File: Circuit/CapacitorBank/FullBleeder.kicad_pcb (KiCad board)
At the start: 2 copper layers, 76.2 x 86.4 mm, 19 parts, among them J1 Signal 1/3, J2 Signal 2/4, J3 Power

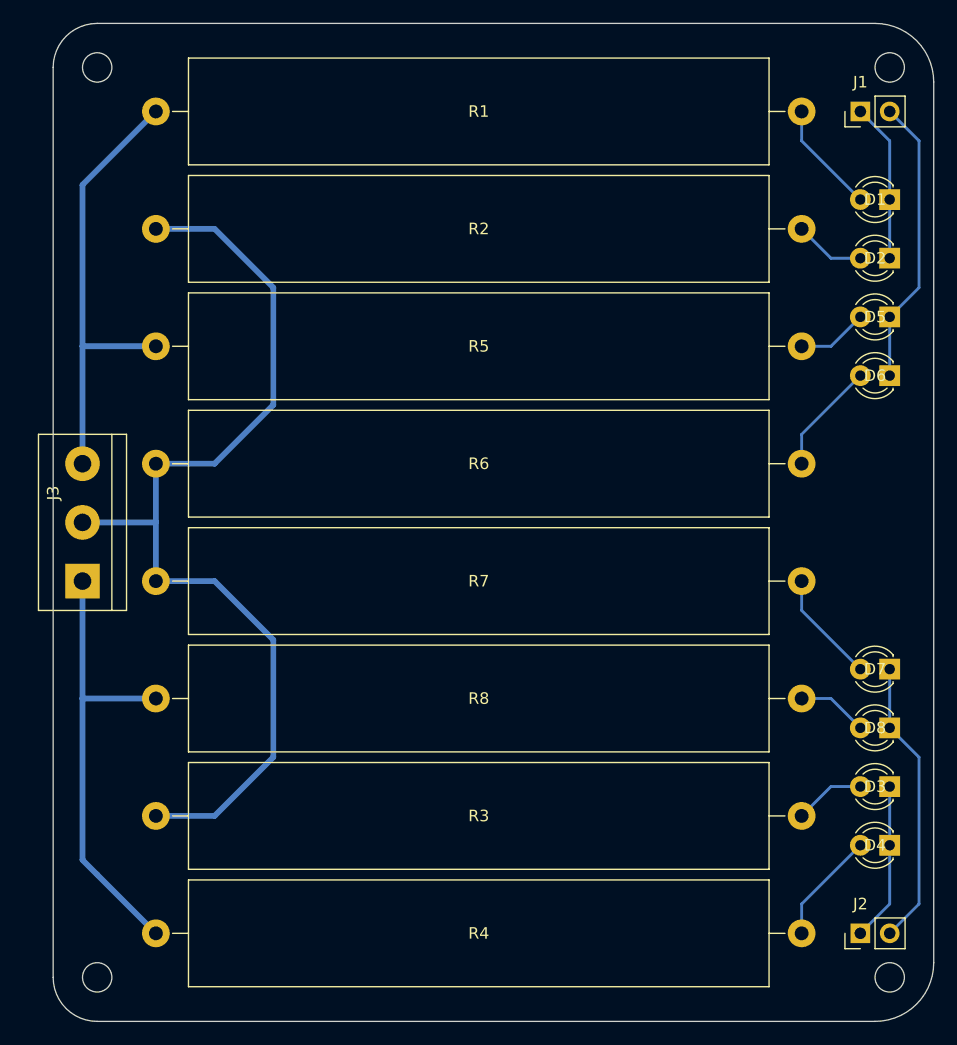
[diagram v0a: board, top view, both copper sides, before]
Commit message: [Circuit] Polarized capacitor bank and bleeder
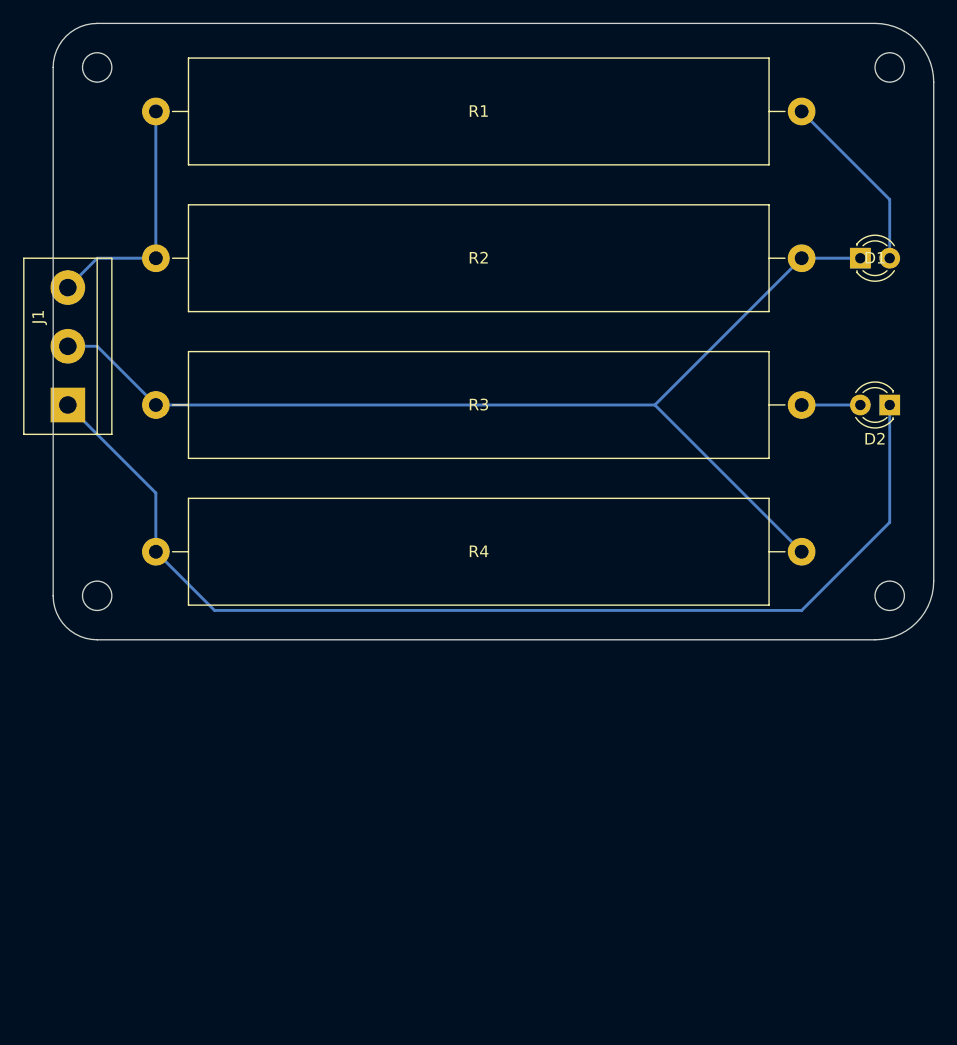
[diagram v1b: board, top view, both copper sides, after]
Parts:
- removed D3, D4, D5, D6, D7, D8: LED, LED_THT:LED_D3.0mm_FlatTop
- removed the J1 at (121.9, 61.0)
- removed J2: Signal 2/4, Connector_PinHeader_2.54mm:PinHeader_1x02_P2.54mm_Vertical
- removed the R2 at (116.8, 71.1)
- removed the R4 at (116.8, 132.1)
- removed R6, R8: 20K, Resistor_THT:R_Axial_Power_L50.0mm_W9.0mm_P55.88mm
- R1, R3: value 20K -> 40K/5W
- R2: renamed from R5; value 20K -> 20K/10W
- R4: renamed from R7; value 20K -> 20K/10W
- moved R4 55.9 mm to (116.8, 99.1), turned to 180 degrees
- moved R3 35.6 mm to (61.0, 86.4)
- moved J1 15.3 mm to (53.3, 86.4)
- moved D2 12.7 mm to (124.5, 86.4)
- moved R2 7.62 mm to (61.0, 73.7)
- moved D1 5.68 mm to (121.9, 73.7), turned to 0 degrees
- renumbered J3 to J1
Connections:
- net +VDC renamed /CapacitorPower+
- D1 pad 1: Net-(D1-Pad1) -> /CapacitorCenter
- D2 pad 1: Net-(D1-Pad1) -> /CapacitorPower-
- J1 pad 1: -VDC -> /CapacitorPower-
- J1 pad 2: GND -> /CapacitorCenter
- R2 pad 2: Net-(D5-Pad2) -> /CapacitorCenter
- R3 pad 1: GND -> /CapacitorCenter
- R3 pad 2: Net-(D3-Pad2) -> Net-(D2-Pad2)
- R4 pad 1: GND -> /CapacitorCenter
- R4 pad 2: Net-(D7-Pad2) -> /CapacitorPower-
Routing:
- net /CapacitorPower-: track 0.00 -> 94.8 mm
- net /CapacitorCenter: track 0.00 -> 93.9 mm
- net GND: track 85.9 -> 0.00 mm
- net -VDC: track 39.5 -> 0.00 mm
- net Net-(D7-Pad1): track 25.0 -> 0.00 mm
- net Net-(D5-Pad1): track 25.0 -> 0.00 mm
- net /CapacitorPower+: track 39.5 -> 21.4 mm
- net Net-(D3-Pad1): track 13.8 -> 0.00 mm
- net Net-(D1-Pad1): track 13.8 -> 0.00 mm
- net Net-(D4-Pad2): track 9.72 -> 0.00 mm
- net Net-(D7-Pad2): track 9.72 -> 0.00 mm
- net Net-(D6-Pad2): track 9.72 -> 0.00 mm
- net Net-(D3-Pad2): track 6.13 -> 0.00 mm
- net Net-(D5-Pad2): track 6.13 -> 0.00 mm
- net Net-(D1-Pad2): track 9.72 -> 15.9 mm
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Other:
- board size 76.2 x 86.4 mm -> 76.2 x 53.3 mm

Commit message: [Circuit] Update the numbers in capacitor bank subsystem
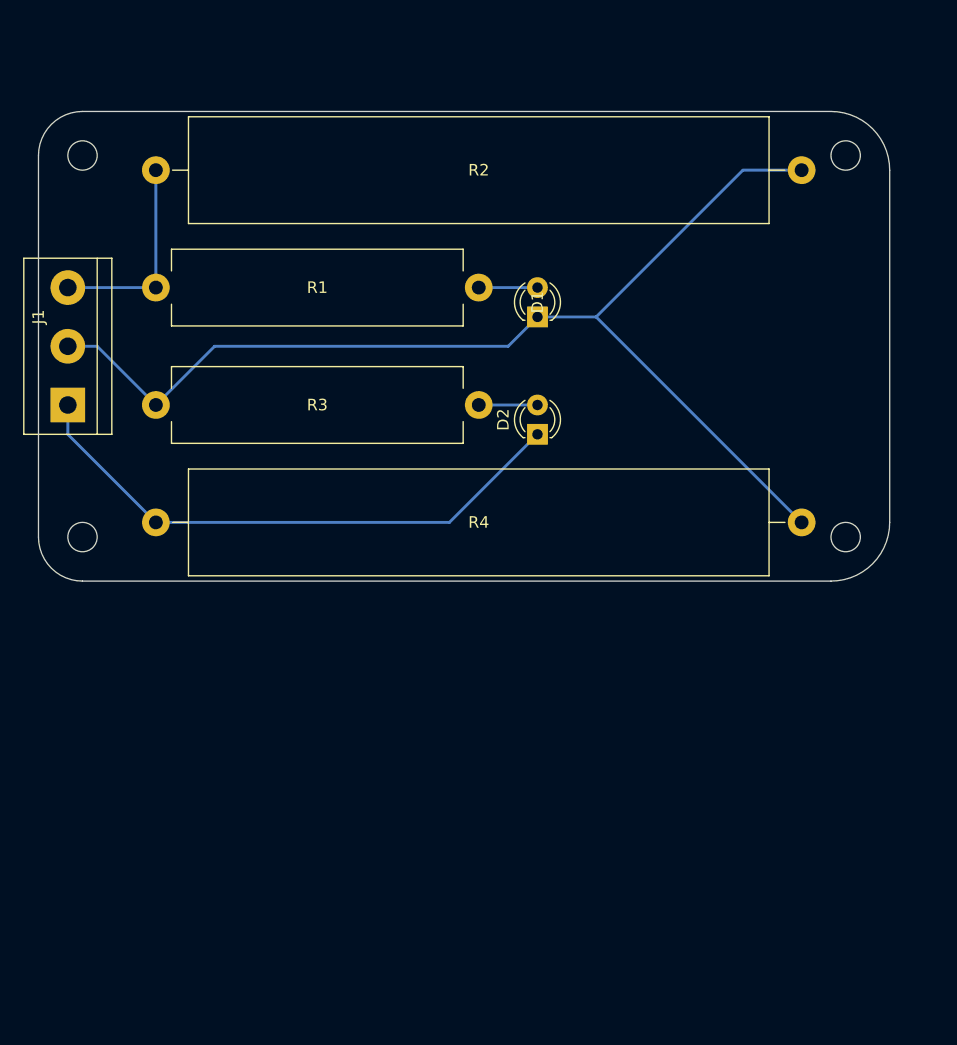
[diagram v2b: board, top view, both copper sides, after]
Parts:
- R1, R3: value 40K/5W -> 43K/5W; footprint Resistor_THT:R_Axial_Power_L50.0mm_W9.0mm_P55.88mm -> Resistor_THT:R_Axial_Power_L25.0mm_W6.4mm_P27.94mm
- moved D2 30.6 mm to (94.0, 88.9), turned to 90 degrees
- moved D1 28.4 mm to (94.0, 78.7), turned to 90 degrees
- moved R1 15.2 mm to (61.0, 76.2)
- moved R2 7.62 mm to (61.0, 66.0)
- moved R4 2.54 mm to (116.8, 96.5)
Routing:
- net /CapacitorPower-: track 94.8 -> 49.5 mm
- net Net-(D1-Pad2): track 15.9 -> 5.08 mm
- net /CapacitorCenter: track 93.9 -> 99.2 mm
- net /CapacitorPower+: track 21.4 -> 17.8 mm
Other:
- board size 76.2 x 53.3 mm -> 73.7 x 40.6 mm

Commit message: [Circuit] Add isolated switches to bleeder circuits
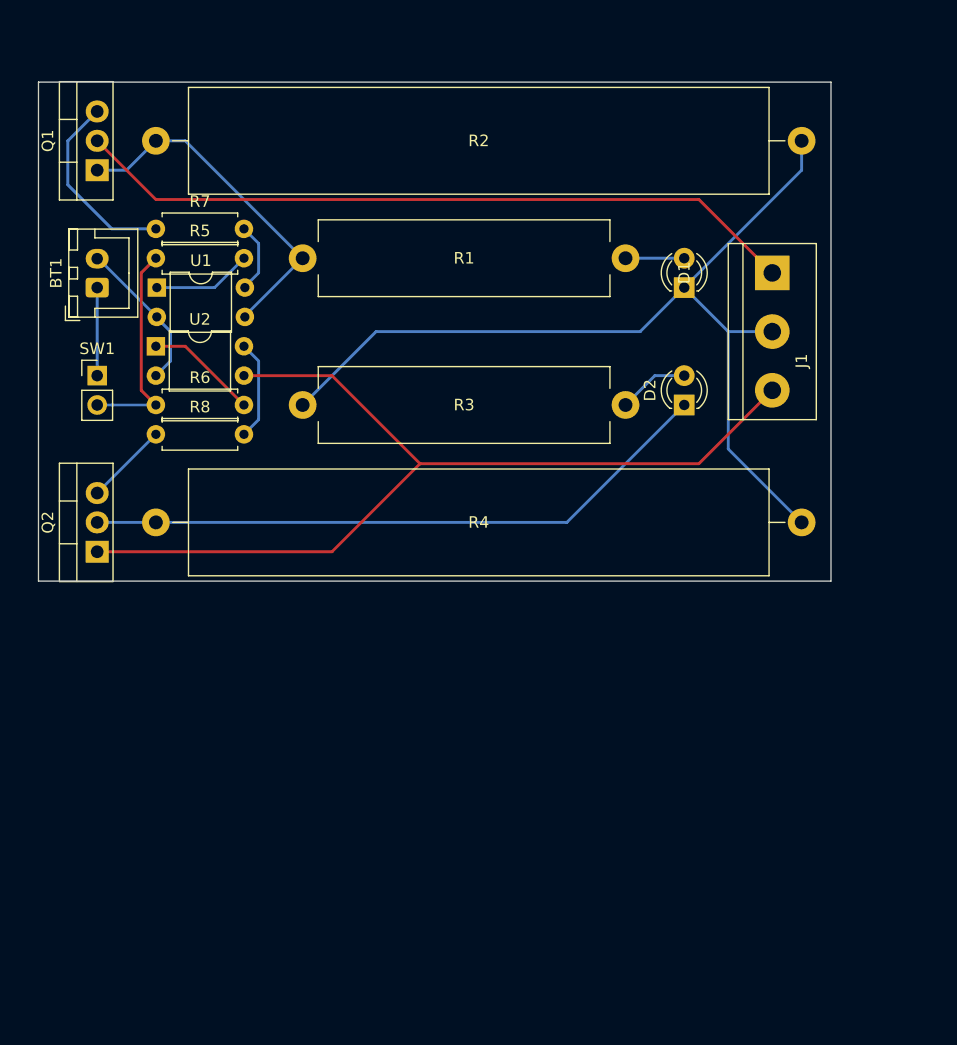
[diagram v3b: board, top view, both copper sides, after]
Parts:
- added BT1: 12V Battery, Connector_JST:JST_XH_B2B-XH-A_1x02_P2.50mm_Vertical, F.Cu at (55.9, 76.2)
- added Q1: BT138-800, Package_TO_SOT_THT:TO-220-3_Vertical, F.Cu at (55.9, 66.0)
- added Q2: BT138-800, Package_TO_SOT_THT:TO-220-3_Vertical, F.Cu at (55.9, 99.1)
- added R5: 1K, Resistor_THT:R_Axial_DIN0207_L6.3mm_D2.5mm_P7.62mm_Horizontal, F.Cu at (61.0, 73.7)
- added R6: 1K, Resistor_THT:R_Axial_DIN0207_L6.3mm_D2.5mm_P7.62mm_Horizontal, F.Cu at (61.0, 86.4)
- added R7: 10K, Resistor_THT:R_Axial_DIN0207_L6.3mm_D2.5mm_P7.62mm_Horizontal, F.Cu at (61.0, 71.1)
- added R8: 10K, Resistor_THT:R_Axial_DIN0207_L6.3mm_D2.5mm_P7.62mm_Horizontal, F.Cu at (61.0, 88.9)
- added SW1: SW_Push, Connector_PinHeader_2.54mm:PinHeader_1x02_P2.54mm_Vertical, F.Cu at (55.9, 83.8)
- added U1: PC817, Package_DIP:DIP-4_W7.62mm, F.Cu at (61.0, 76.2)
- added U2: PC817, Package_DIP:DIP-4_W7.62mm, F.Cu at (61.0, 81.3)
- moved J1 62.0 mm to (114.3, 74.9), turned to 270 degrees
- moved D2 13.0 mm to (106.7, 86.4)
- moved D1 13.0 mm to (106.7, 76.2)
- moved R1 13.0 mm to (73.7, 73.7)
- moved R3 12.7 mm to (73.7, 86.4)
- moved R2 2.54 mm to (61.0, 63.5)
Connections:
- D2 pad 1: /CapacitorPower- -> Net-(D2-Pad1)
- J1 pad 1: /CapacitorPower- -> /CapacitorPower+
- J1 pad 3: /CapacitorPower+ -> /CapacitorPower-
- R1 pad 1: /CapacitorPower+ -> Net-(Q1-Pad1)
- R2 pad 1: /CapacitorPower+ -> Net-(Q1-Pad1)
- R4 pad 2: /CapacitorPower- -> Net-(D2-Pad1)
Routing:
- net Net-(D2-Pad1): track 0.00 -> 55.0 mm
- net /CapacitorPower+: track 17.8 -> 63.2 mm
- net /CapacitorPower-: track 49.5 -> 82.6 mm
- net Net-(Q1-Pad1): track 0.00 -> 30.3 mm
- net Net-(R5-Pad1): track 0.00 -> 18.8 mm
- net /CapacitorCenter: track 99.2 -> 82.5 mm
- net Net-(Q1-Pad3): track 0.00 -> 16.6 mm
- net Net-(BT1-Pad2): track 0.00 -> 13.3 mm
- net Net-(R6-Pad2): track 0.00 -> 9.72 mm
- net Net-(R8-Pad2): track 0.00 -> 8.67 mm
- net Net-(R5-Pad2): track 0.00 -> 8.59 mm
- net Net-(BT1-Pad1): track 0.00 -> 7.62 mm
- net Net-(Q2-Pad3): track 0.00 -> 7.18 mm
- net Net-(R7-Pad2): track 0.00 -> 6.18 mm
- net Net-(D2-Pad2): track 5.08 -> 6.13 mm
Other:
- board size 73.7 x 40.6 mm -> 68.6 x 43.2 mm
